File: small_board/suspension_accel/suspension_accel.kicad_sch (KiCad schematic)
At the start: 23 parts, among them IC1 TJA1050T_CM,118, IC2 AMS1117-3.3, IC3 ESP32-S3-MINI-1-N8, IC4 LSM6DSV16BXTR, IC5 ADS1220IPWR, IC6 TLV75533PDBVR, J1 OSTTE040104, J2 BM04B-GVHS-TB_LF__SN_, J3 BM04B-GVHS-TB_LF__SN_, J4 BM04B-GVHS-TB_LF__SN_

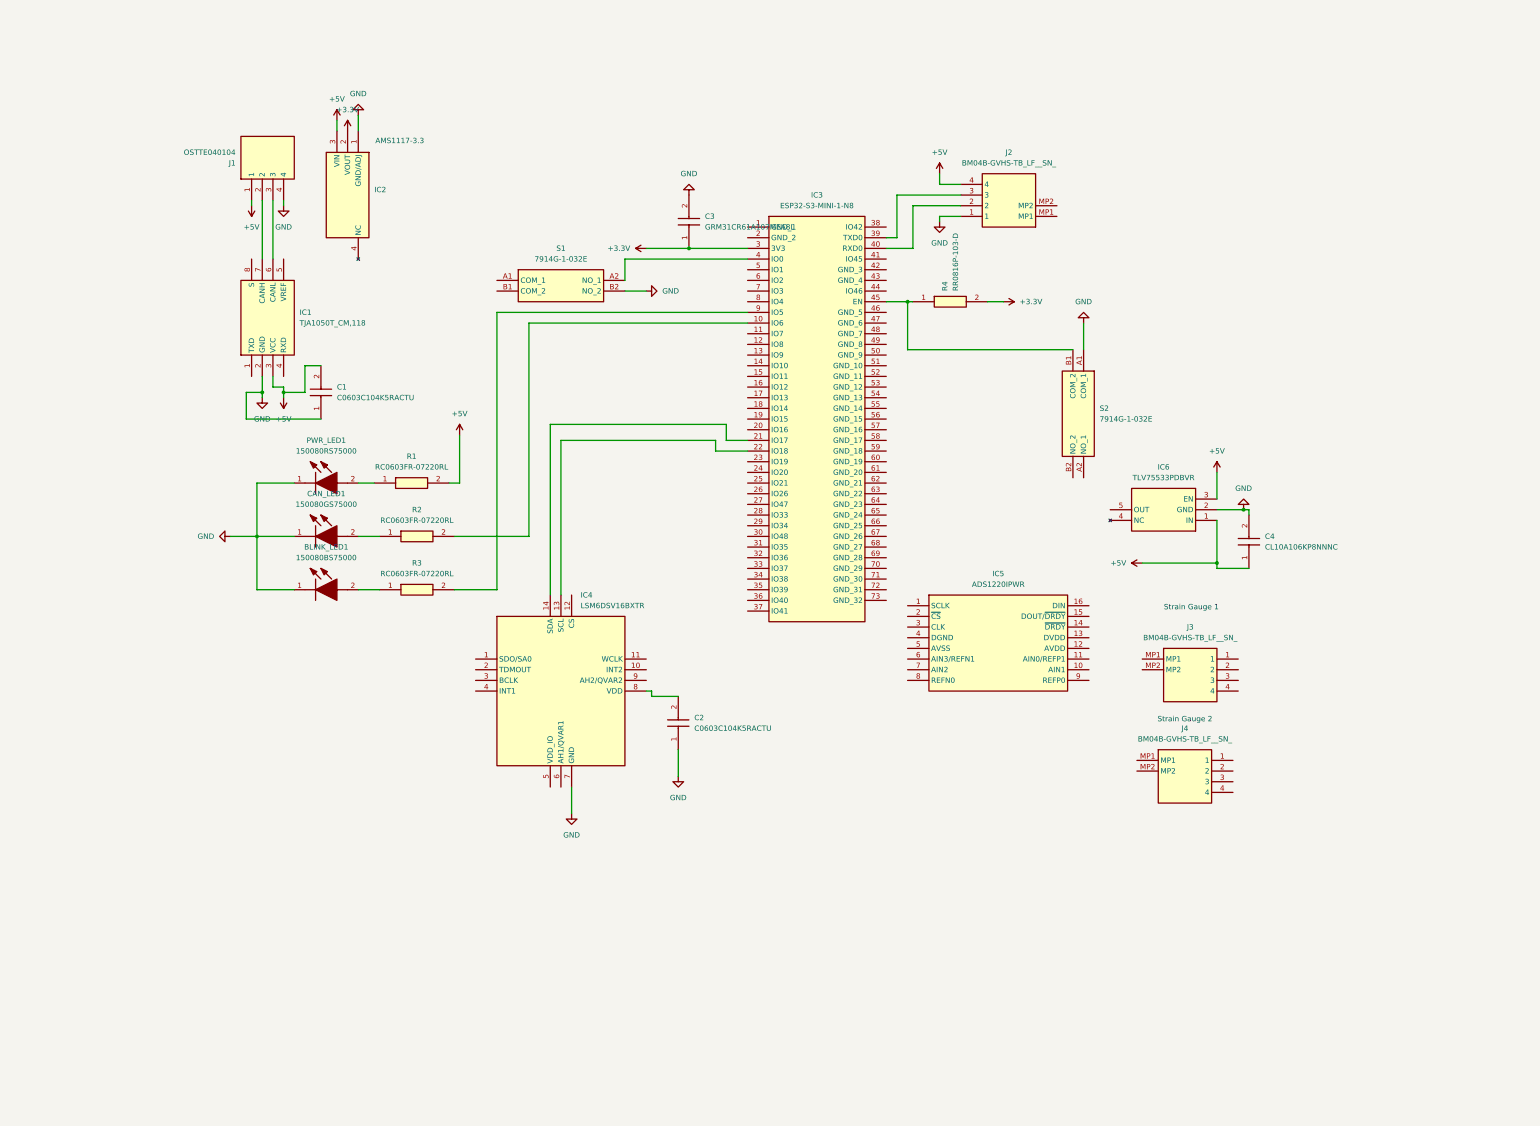
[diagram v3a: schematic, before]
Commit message: Added rev polarity protection, ads1220, routed, tja1050 level shifter, etc...
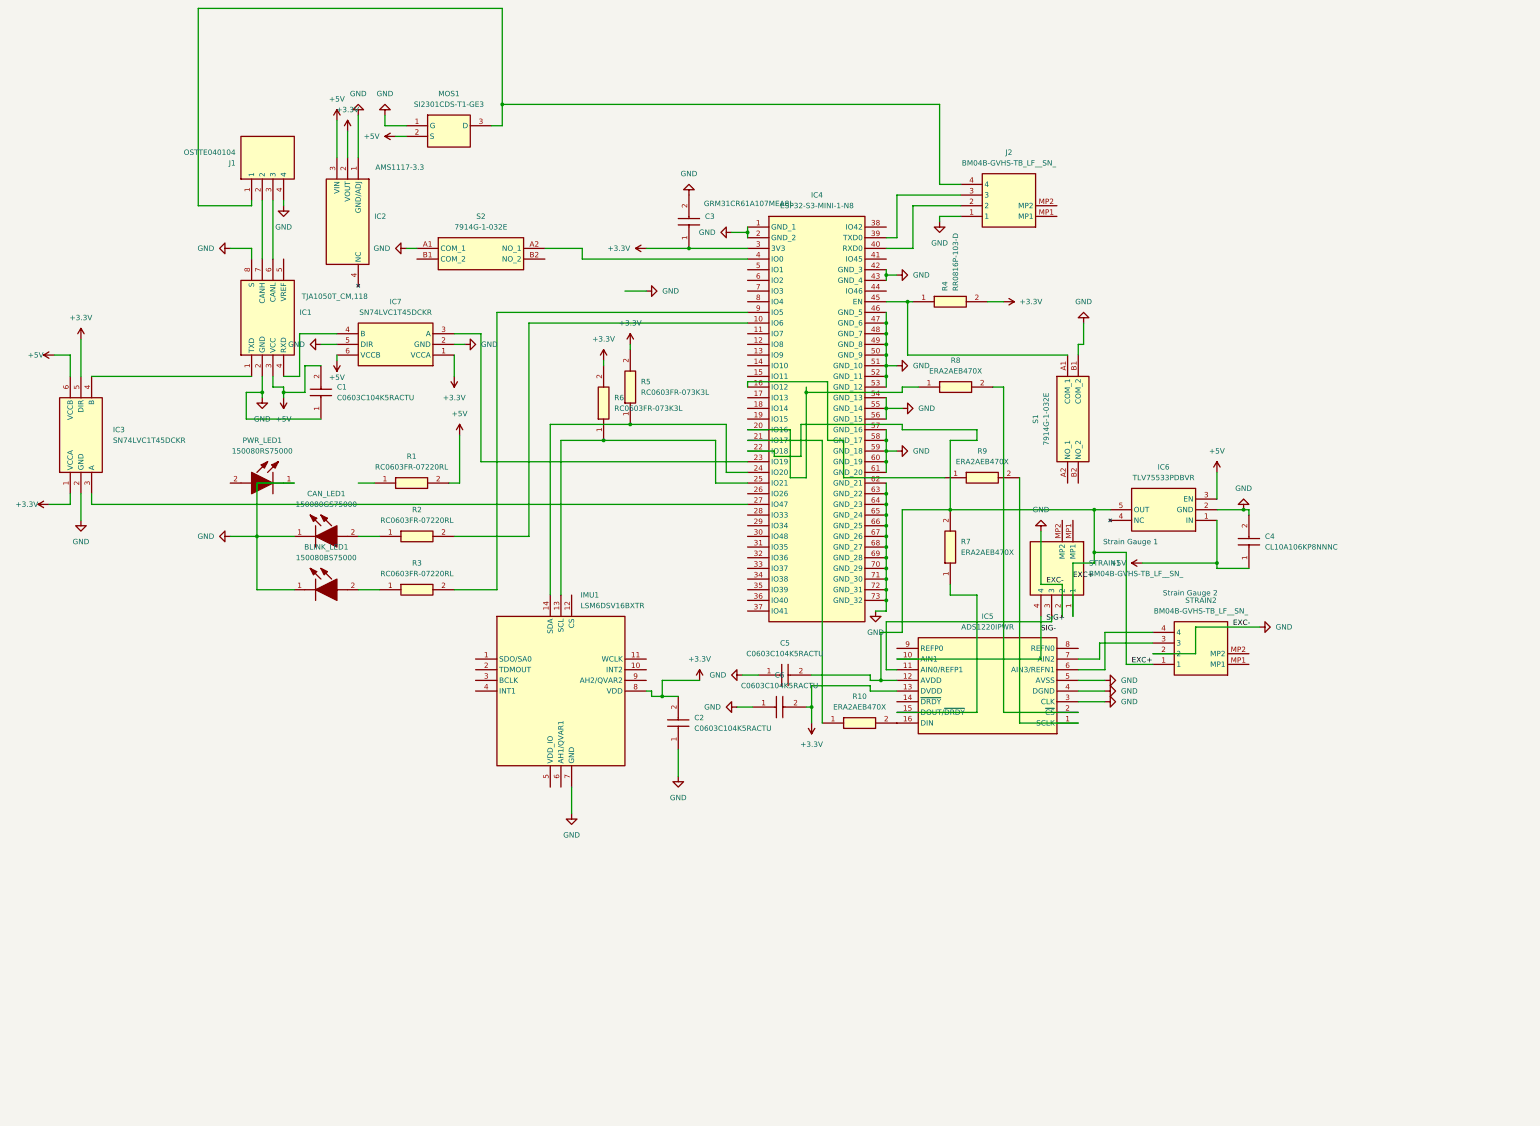
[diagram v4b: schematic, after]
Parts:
- added C5, C6: C0603C104K5RACTU, C0603, symbol C0603C104K5RACTU:C0603C104K5RACTU
- added IC3, IC7: SN74LVC1T45DCKR, SOT65P210X110-6N, symbol SN74LVC1T45DCKR:SN74LVC1T45DCKR
- added MOS1: SI2301CDS-T1-GE3, SOT95P237X112-3N, symbol SI2301CDS-T1-GE3:SI2301CDS-T1-GE3
- added R10, R7, R8, R9: ERA2AEB470X, ERA2AED122X, symbol ERA2AEB470X:ERA2AEB470X
- added R5, R6: RC0603FR-073K3L, RESC1608X55N, symbol RC0603FR-073K3L:RC0603FR-073K3L
- renumbered IC3 to IC4, IC4 to IMU1, J3 to STRAIN1, J4 to STRAIN2
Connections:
- net +3.3V: now also C2.2, IC5.13 (DVDD), IMU1.8 (VDD), C6.2, IC3.1 (VCCA), IC3.5 (DIR), IC7.1 (VCCA), R5.2, R6.2
- net +5V: now also IC3.6 (VCCB), IC7.6 (VCCB), MOS1.2 (S); no longer J1.1, J2.4
- net GND: now also IC1.8 (S), IC4.1 (GND_1), IC4.2 (GND_2), IC4.42 (GND_3), IC4.43 (GND_4), IC4.46 (GND_5), IC4.47 (GND_6), IC4.48 (GND_7), IC4.49 (GND_8), IC4.50 (GND_9), IC4.51 (GND_10), IC4.52 (GND_11), IC4.53 (GND_12), IC4.54 (GND_13), IC4.55 (GND_14), IC4.56 (GND_15), IC4.57 (GND_16), IC4.58 (GND_17), IC4.59 (GND_18), IC4.60 (GND_19), IC4.61 (GND_20), IC4.62 (GND_21), IC4.63 (GND_22), IC4.64 (GND_23), IC4.65 (GND_24), IC4.66 (GND_25), IC4.67 (GND_26), IC4.68 (GND_27), IC4.69 (GND_28), IC4.70 (GND_29), IC4.71 (GND_30), IC4.72 (GND_31), IC4.73 (GND_32), IC5.3 (CLK), IC5.4 (DGND), IC5.5 (AVSS), S1.B1 (COM_2), STRAIN1.2, STRAIN2.2, C5.1, C6.1, IC3.2 (GND), IC7.2 (GND), IC7.5 (DIR), MOS1.1 (G); no longer S1.B2 (NO_2)
- net at IMU1.13 (SCL): now also IC4.25 (IO21), R6.1; no longer IC4.22 (IO18)
- net at IMU1.14 (SDA): now also IC4.24 (IO20), R5.1; no longer IC4.21 (IO17)
- net at PWR_LED1.2 (A): no longer R1.1
- net at IC5.1 (SCLK): now also R9.2
- net SIG-: now reaches IC5.10 (AIN1)
- net SIG-: now also STRAIN1.4
- net SIG+: now reaches IC5.11 (AIN0/REFP1)
- net SIG+: now also STRAIN1.3
- net EXC+: now reaches IC5.12 (AVDD)
- net EXC+: now also IC4.22 (IO18), IC6.5 (OUT), STRAIN1.1, STRAIN2.1, C5.2, R7.2
- net at IC5.15 (DOUT/~{DRDY}): now also R7.1
- net at IC5.16 (DIN): now also R10.2
- net at IC5.2 (~{CS}): now also R8.2
- net at IC5.6 (AIN3/REFN1): now also STRAIN2.4
- net at IC5.7 (AIN2): now also STRAIN2.3
- net at IC1.1 (TXD): now also IC3.4 (B)
- net at IC1.4 (RXD): now also IC7.4 (B)
- net at S1.A1 (COM_1): now also IC4.45 (EN), R4.1 (R1)
- net at S1.A2 (NO_1): no longer IC4.4 (IO0)
- net at S2.A2 (NO_1): now also IC4.4 (IO0)
- net at IC4.16 (IO12): now also R9.1
- net at IC4.20 (IO16): now also R8.1
- net at IC4.23 (IO19): now also IC7.3 (A)
- net at IC4.27 (IO47): now also IC3.3 (A)
- new net: J1.1, J2.4, MOS1.3 (D)
- new net: IC4.21 (IO17), R10.1
- now unconnected: S2.B1 (COM_2)
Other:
- moved on the sheet: IC2, IC5, PWR_LED1, S1, S2, STRAIN1, STRAIN2

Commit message: finished filter work, rerounted connection, bus level shifters connected, blink led connected, etc...
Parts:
- removed CAN_LED1: 150080GS75000, LEDM2012X70N, symbol 150080GS75000:150080GS75000
- removed R2: RC0603FR-07220RL, RESC1608X55N, symbol RC0603FR-07220RL:RC0603FR-07220RL
- added C7, C8: C0603C103F3GECTU, CAPC1608X87N, symbol C0603C103F3GECTU:C0603C103F3GECTU
- added R11, R12, R13, R14: ERA-2AEB101X, ERA2AED122X, symbol ERA-2AEB101X:ERA-2AEB101X
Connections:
- net SIG+: no longer IC5.11 (AIN0/REFP1), STRAIN1.3
- net SIG-: no longer IC5.10 (AIN1), STRAIN1.4
- net at PWR_LED1.2 (A): now also R1.1
- net at IC5.6 (AIN3/REFN1): now also C7.1, R11.1; no longer STRAIN2.4
- net at IC5.7 (AIN2): now also C7.2, R12.1; no longer STRAIN2.3
- net at IC4.38 (IO42): now also R3.2
- net at IC4.9 (IO5): no longer R3.2
- new net: C8.1, IC5.11 (AIN0/REFP1), R13.1
- new net: C8.2, IC5.10 (AIN1), R14.1
- new net: R13.2, STRAIN1.4
- new net: R12.2, STRAIN2.3
- new net: R11.2, STRAIN2.4
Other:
- moved on the sheet: PWR_LED1, STRAIN2

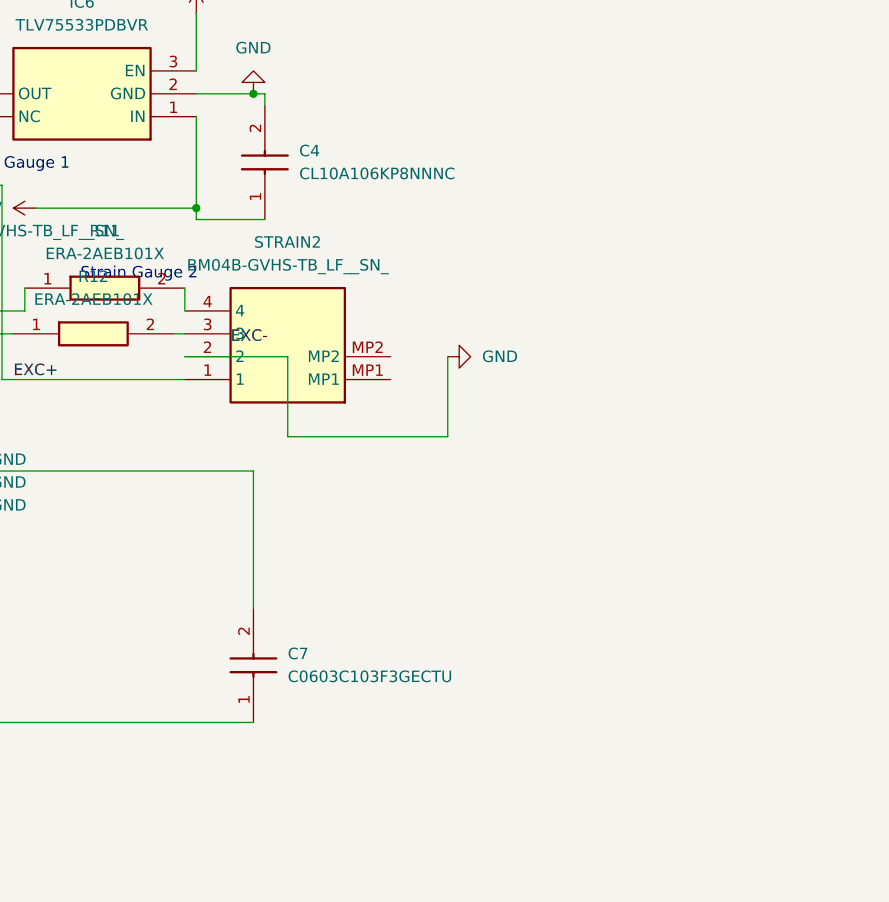
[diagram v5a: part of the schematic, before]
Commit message: added matched resistor network
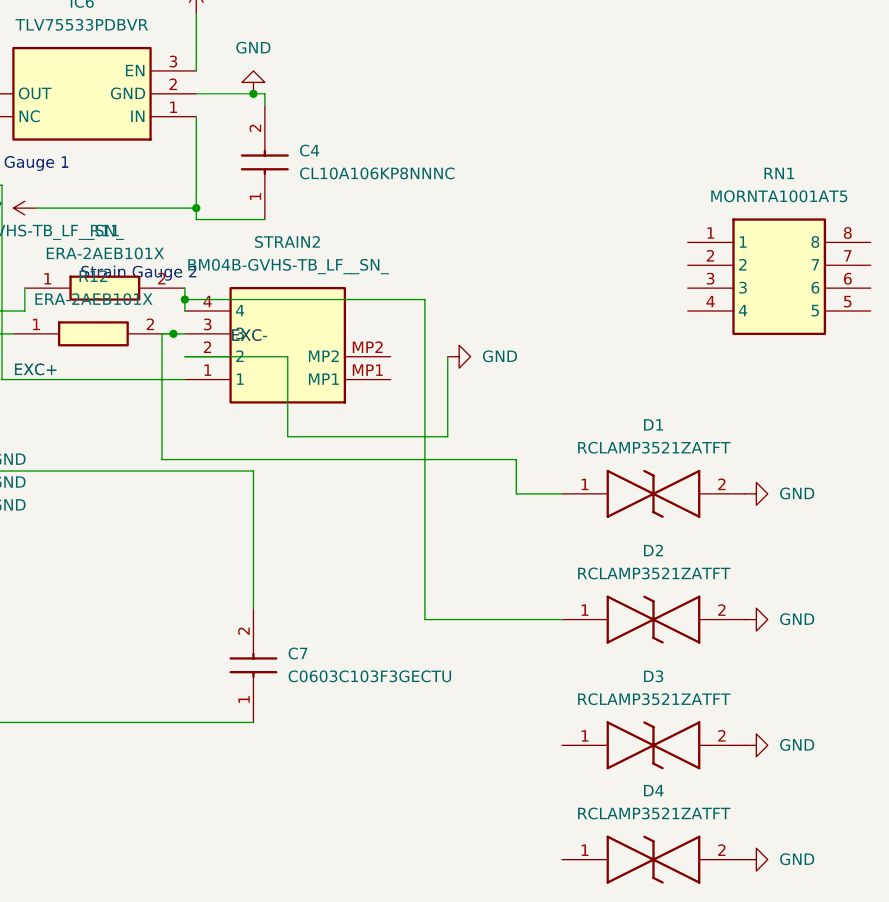
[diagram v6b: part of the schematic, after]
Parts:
- added D1, D2, D3, D4: RCLAMP3521ZATFT, RCLAMP3521ZATFT, symbol RCLAMP3521ZATFT:RCLAMP3521ZATFT
- added RN1: MORNTA1001AT5, MORNTA1001AT5, symbol MORNTA1001AT5:MORNTA1001AT5
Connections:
- net GND: now also D1.2, D2.2, D3.2, D4.2
- net at R12.2, STRAIN2.3: now also D1.1
- net at R11.2, STRAIN2.4: now also D2.1

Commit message: started laying out final components
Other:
- moved on the sheet: RN1
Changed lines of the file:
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@@
 	(symbol
 		(lib_id "MORNTA1001AT5:MORNTA1001AT5")
-		(at 317.5 127 0)
-		(unit 1)
-		(exclude_from_sim no)
-		(in_bom yes)
-		(on_board yes)
-		(dnp no)
-		(fields_autoplaced yes)
+		(at 231.14 190.5 0)
+		(unit 1)
+		(exclude_from_sim no)
+		(in_bom yes)
+		(on_board yes)
+		(dnp no)
 		(property "Reference" "RN1"
-			(at 327.66 119.38 0)
+			(at 241.3 182.88 0)
 			(effects
 				(font
@@
 		)
 		(property "Value" "MORNTA1001AT5"
-			(at 327.66 121.92 0)
+			(at 241.3 185.42 0)
 			(effects
 				(font
@@
 		)
 		(property "Footprint" "MORNTA1001AT5"
-			(at 334.01 221.92 0)
+			(at 247.65 285.42 0)
 			(effects
 				(font
@@
 		)
 		(property "Datasheet" "https://www.vishay.com/docs/60129/morn.pdf"
-			(at 334.01 321.92 0)
+			(at 247.65 385.42 0)
 			(effects
 				(font
@@
 		)
 		(property "Description" "1k Ohm +/-0.1% 50mW Power Per Element Isolated 4 Resistor Network/Array +/-25ppm/C 8-TSSOP, 8-MSOP (0.118\", 3.00mm Width)"
-			(at 317.5 127 0)
+			(at 231.14 190.5 0)
 			(effects
 				(font
@@
 		)
 		(property "Height" "1.1"
-			(at 334.01 521.92 0)
+			(at 247.65 585.42 0)
 			(effects
 				(font
@@
 		)
 		(property "Manufacturer_Name" "Vishay"
-			(at 334.01 621.92 0)
+			(at 247.65 685.42 0)
 			(effects
 				(font
@@
 		)
 		(property "Manufacturer_Part_Number" "MORNTA1001AT5"
-			(at 334.01 721.92 0)
+			(at 247.65 785.42 0)
 			(effects
 				(font
@@
 		)
 		(property "Mouser Part Number" "71-MORNTA1001AT5"
-			(at 334.01 821.92 0)
+			(at 247.65 885.42 0)
 			(effects
 				(font
@@
 		)
 		(property "Mouser Price/Stock" "https://www.mouser.co.uk/ProductDetail/Vishay-Thin-Film/MORNTA1001AT5?qs=mlqvmmZDxoUQbRHGbp0kiA%3D%3D"
-			(at 334.01 921.92 0)
+			(at 247.65 985.42 0)
 			(effects
 				(font
@@
 		)
 		(property "Arrow Part Number" ""
-			(at 334.01 1021.92 0)
+			(at 247.65 1085.42 0)
 			(effects
 				(font
@@
 		)
 		(property "Arrow Price/Stock" ""
-			(at 334.01 1121.92 0)
+			(at 247.65 1185.42 0)
 			(effects
 				(font
@@
 		(on_board yes)
 		(dnp no)
-		(fields_autoplaced yes)
 		(property "Reference" "C4"
 			(at 274.32 116.8399 90)
